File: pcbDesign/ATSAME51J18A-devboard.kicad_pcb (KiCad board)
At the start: 2 copper layers, 83.6 x 28.4 mm, 75 parts, among them IC1 MP9361DJ-LF-P, J1 Micro_SD_Card, J10 CAN, J11 Conn_01x32_Male, J2 USB C, J3 QWIIC, J4 S2B-PH-K-S(LF)(SN), J7 Conn_01x32_Male, SW1 RST, U1 TCAN1051GVDRQ1, U2 ATSAME51J18A-A, U3 MIC5219-5.0YMM, U4 LM27762, U5 TPS60501DGS, U7 BQ24074RGT, U8 BQ27441DRZR-G1B, Y1 32.768

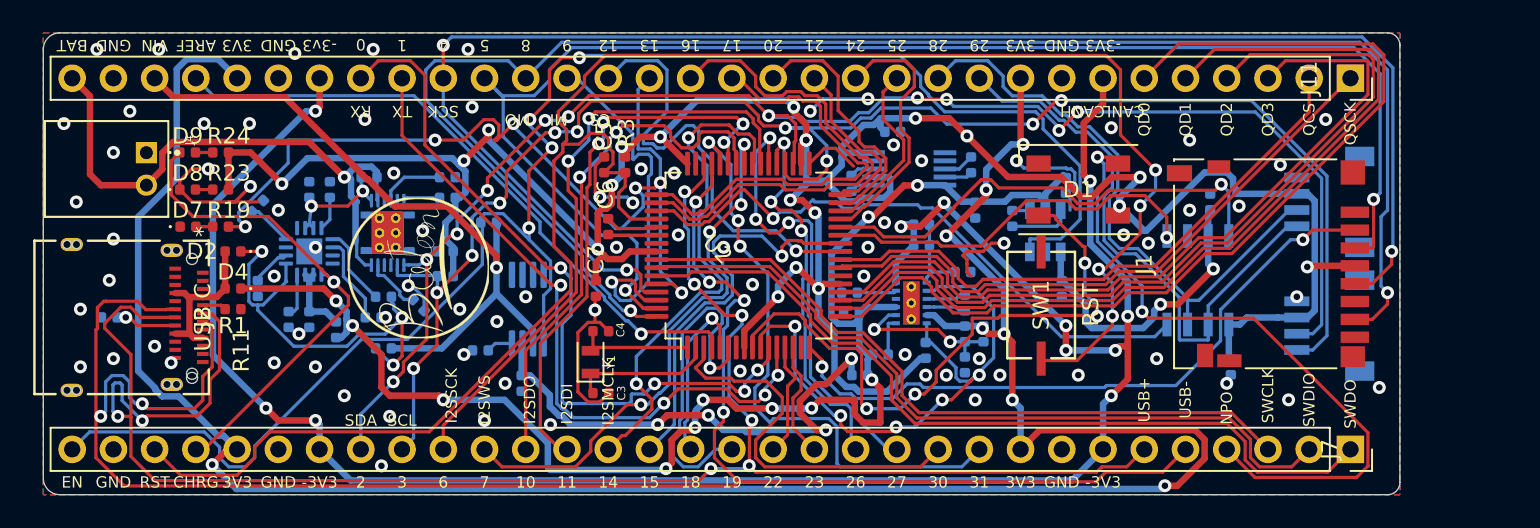
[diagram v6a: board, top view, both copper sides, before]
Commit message: Fixed some DRC errors
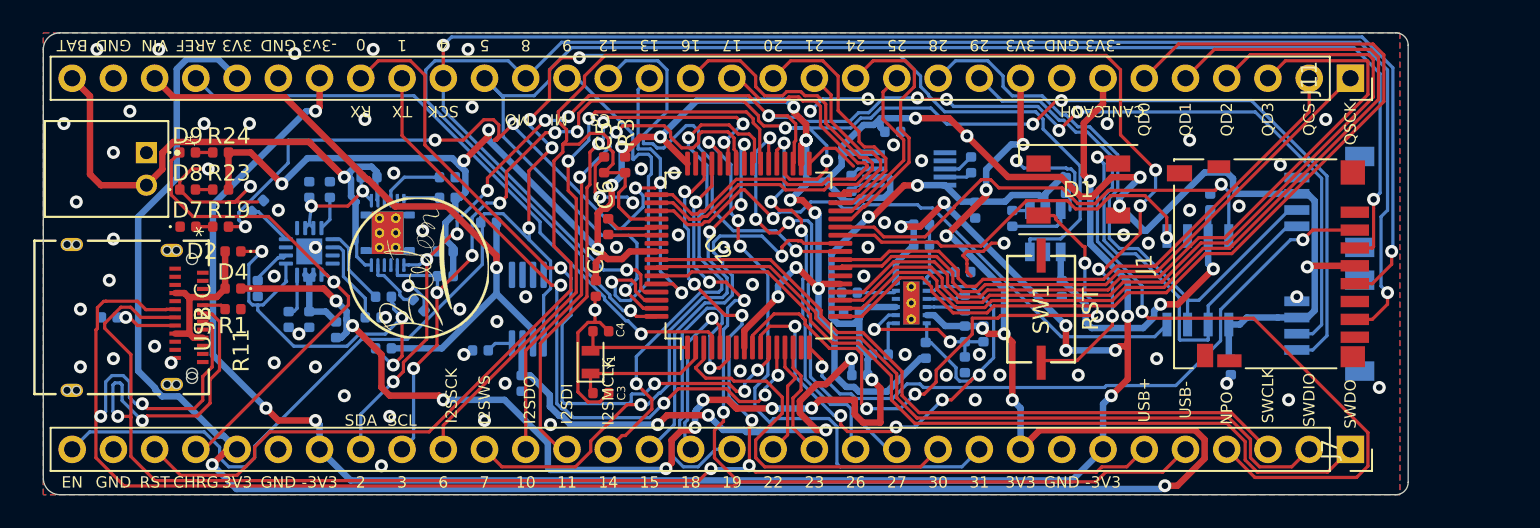
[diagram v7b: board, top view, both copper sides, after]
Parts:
- moved SW1 0.25 mm to (202.4, 128.5)
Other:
- board size 83.6 x 28.4 mm -> 84.1 x 28.4 mm
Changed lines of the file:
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@@
-(kicad_pcb (version 20171130) (host pcbnew "(5.1.6)-1")
+(kicad_pcb (version 20171130) (host pcbnew 5.1.5+dfsg1-2build2)
   (general
     (thickness 1.6)
     (drawings 93)
-    (tracks 2020)
+    (tracks 2019)
     (zones 0)
     (modules 75)
@@
   )
   (module "PTS636:PTS636 SM25F SMTR LFS" (layer F.Cu)
-    (at 202.438 128.27 90)
+    (at 202.438 128.524 90)
     (fp_text reference SW1 (at 0 0 90) (layer F.SilkS)
       (effects (font (size 1 1) (thickness 0.15)))
@@
   (gr_arc (start 141.986 112.522) (end 141.986 111.506) (angle -90) (layer Edge.Cuts) (width 0.05))
   (gr_arc (start 141.986 138.938) (end 140.97 138.938) (angle -90) (layer Edge.Cuts) (width 0.05))
-  (gr_line (start 141.986 111.506) (end 223.774 111.506) (layer Edge.Cuts) (width 0.05))
-  (gr_arc (start 223.774 139.192) (end 223.774 139.954) (angle -90) (layer Edge.Cuts) (width 0.05))
-  (gr_arc (start 223.774 112.268) (end 224.536 112.268) (angle -90) (layer Edge.Cuts) (width 0.05))
+  (gr_line (start 141.986 111.506) (end 224.282 111.506) (layer Edge.Cuts) (width 0.05))
+  (gr_arc (start 224.282 139.192) (end 224.282 139.954) (angle -90) (layer Edge.Cuts) (width 0.05))
+  (gr_arc (start 224.282 112.268) (end 225.044 112.268) (angle -90) (layer Edge.Cuts) (width 0.05))
   (gr_line (start 140.97 138.938) (end 140.97 112.522) (layer Edge.Cuts) (width 0.05))
-  (gr_line (start 223.774 139.954) (end 141.986 139.954) (layer Edge.Cuts) (width 0.05))
-  (gr_line (start 224.536 112.268) (end 224.536 139.192) (layer Edge.Cuts) (width 0.05))
+  (gr_line (start 224.282 139.954) (end 141.986 139.954) (layer Edge.Cuts) (width 0.05))
+  (gr_line (start 225.044 112.268) (end 225.044 139.192) (layer Edge.Cuts) (width 0.05))
   (via (at 193.344907 118.406298) (size 0.8) (drill 0.4) (layers F.Cu B.Cu) (net 1))
   (via (at 218.186 127.762) (size 0.8) (drill 0.4) (layers F.Cu B.Cu) (net 1))
@@
   (via (at 211.582 122.428) (size 0.8) (drill 0.4) (layers F.Cu B.Cu) (net 1))
   (via (at 214.63 122.174) (size 0.8) (drill 0.4) (layers F.Cu B.Cu) (net 1))
-  (via (at 206.756 117.348) (size 0.8) (drill 0.4) (layers F.Cu B.Cu) (net 1))
+  (via (at 206.502 117.094) (size 0.8) (drill 0.4) (layers F.Cu B.Cu) (net 1))
   (via (at 191.516 126.492) (size 0.8) (drill 0.4) (layers F.Cu B.Cu) (net 1))
   (via (at 194.056 131.318) (size 0.8) (drill 0.4) (layers F.Cu B.Cu) (net 1))
@@
   (via (at 196.596 132.588) (size 0.8) (drill 0.4) (layers F.Cu B.Cu) (net 1))
   (via (at 195.326 132.588) (size 0.8) (drill 0.4) (layers F.Cu B.Cu) (net 1))
-  (via (at 198.628 131.572) (size 0.8) (drill 0.4) (layers F.Cu B.Cu) (net 1))
+  (via (at 198.628 131.318) (size 0.8) (drill 0.4) (layers F.Cu B.Cu) (net 1))
   (via (at 183.896 132.334) (size 0.8) (drill 0.4) (layers F.Cu B.Cu) (net 1))
   (via (at 191.77 124.714) (size 0.8) (drill 0.4) (layers F.Cu B.Cu) (net 1))
@@
   (segment (start 180.647367 123.318255) (end 181.533091 123.318255) (width 0.2) (layer F.Cu) (net 75))
   (segment (start 178.7415 122.472) (end 179.801112 122.472) (width 0.2) (layer F.Cu) (net 75))
-  (segment (start 187.622504 122.536001) (end 186.327999 122.536001) (width 0.2) (layer B.Cu) (net 75))
-  (segment (start 188.354493 121.804012) (end 187.622504 122.536001) (width 0.2) (layer B.Cu) (net 75))
+  (segment (start 190.208076 122.31102) (end 189.817056 121.92) (width 0.2) (layer B.Cu) (net 75))
   (segment (start 186.327999 122.536001) (end 185.928 122.936) (width 0.2) (layer B.Cu) (net 75))
-  (segment (start 188.425872 121.804012) (end 188.354493 121.804012) (width 0.2) (layer B.Cu) (net 75))
-  (segment (start 209.434139 130.221011) (end 203.674955 130.221011) (width 0.2) (layer B.Cu) (net 75))
-  (segment (start 210.185 129.47015) (end 209.434139 130.221011) (width 0.2) (layer B.Cu) (net 75))
-  (segment (start 195.025038 122.293002) (end 194.825047 122.093011) (width 0.2) (layer B.Cu) (net 75))
-  (segment (start 191.517933 122.093011) (end 191.299923 122.311021) (width 0.2) (layer B.Cu) (net 75))
-  (segment (start 203.674955 130.221011) (end 195.746946 122.293002) (width 0.2) (layer B.Cu) (net 75))
-  (segment (start 195.746946 122.293002) (end 195.025038 122.293002) (width 0.2) (layer B.Cu) (net 75))
-  (segment (start 189.817056 121.92) (end 188.468 121.92) (width 0.2) (layer B.Cu) (net 75))
   (segment (start 191.299923 122.311021) (end 190.208076 122.31102) (width 0.2) (layer B.Cu) (net 75))
-  (segment (start 190.208076 122.31102) (end 189.817056 121.92) (width 0.2) (layer B.Cu) (net 75))
+  (segment (start 188.238505 121.92) (end 187.622504 122.536001) (width 0.2) (layer B.Cu) (net 75))
   (segment (start 194.825047 122.093011) (end 191.517933 122.093011) (width 0.2) (layer B.Cu) (net 75))
+  (segment (start 187.622504 122.536001) (end 186.327999 122.536001) (width 0.2) (layer B.Cu) (net 75))
+  (segment (start 191.517933 122.093011) (end 191.299923 122.311021) (width 0.2) (layer B.Cu) (net 75))
+  (segment (start 195.025038 122.293002) (end 194.825047 122.093011) (width 0.2) (layer B.Cu) (net 75))
+  (segment (start 195.746946 122.293002) (end 195.025038 122.293002) (width 0.2) (layer B.Cu) (net 75))
+  (segment (start 203.674955 130.221011) (end 195.746946 122.293002) (width 0.2) (layer B.Cu) (net 75))
+  (segment (start 209.434139 130.221011) (end 203.674955 130.221011) (width 0.2) (layer B.Cu) (net 75))
+  (segment (start 189.817056 121.92) (end 188.238505 121.92) (width 0.2) (layer B.Cu) (net 75))
+  (segment (start 210.185 129.47015) (end 209.434139 130.221011) (width 0.2) (layer B.Cu) (net 75))
   (segment (start 213.995 121.297148) (end 213.531466 120.833614) (width 0.2) (layer B.Cu) (net 76))
   (via (at 213.531466 120.833614) (size 0.8) (drill 0.4) (layers F.Cu B.Cu) (net 76))

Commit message: Finnished routing board prototype(v0.2)
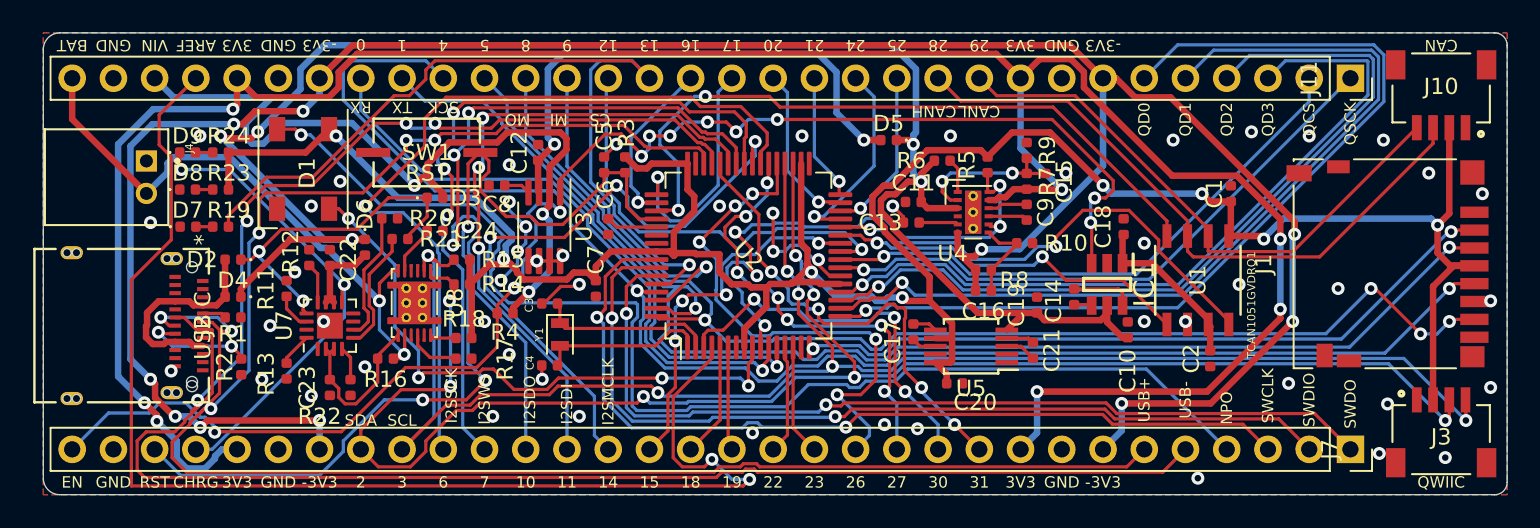
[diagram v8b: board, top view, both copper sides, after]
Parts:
- C1, C10, C11, C12, C13, C14, C15, C16, C17, C18, C19, C2, C20, C21, C22, C23, C24, C8, C9, D3, D5, D6, IC1, J10, J3, R10, R11, R12, R13, R14, R15, R16, R17, R18, R2, R20, R21, R22, R4, R5, R6, R7, R8, R9, U1, U3, U4, U5, U7, U8: moved to F.Cu
- G***: moved to B.Cu
- moved D1 47.8 mm to (157.0, 119.9), turned to 270 degrees
- moved SW1 39.1 mm to (164.6, 118.9), turned to 180 degrees
- moved G*** 20.6 mm to (184.7, 125.2), turned to 270 degrees
- moved C20 16.0 mm to (197.1, 133.1)
- moved D5 14.6 mm to (193.0, 118.1)
- moved C12 14.3 mm to (171.4, 118.9), turned to 90 degrees
- moved R9 13.7 mm to (201.5, 118.7), turned to 90 degrees
- moved R6 12.5 mm to (196.3, 119.4)
- moved R22 12.3 mm to (159.9, 133.3), turned to 90 degrees
- moved C23 12.3 mm to (158.6, 133.3), turned to 270 degrees
- moved C21 12.0 mm to (201.9, 131.1), turned to 270 degrees
- moved R5 12.0 mm to (199.1, 119.6), turned to 90 degrees
- moved U5 11.6 mm to (198.1, 130.8)
- moved R16 11.2 mm to (162.1, 131.6)
- moved R17 11.2 mm to (166.9, 131.6)
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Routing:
- net RST: track 116.0 -> 57.5 mm, vias 4 -> 3
- net AREF: track 39.7 -> 79.1 mm, vias 1 -> 2
- net NEOPIXEL_DOUT: track 41.2 -> 76.0 mm, vias 2 -> 1
- net GND: track 48.5 -> 21.7 mm, vias 81 -> 54
- net 8[MI]: track 100.8 -> 75.1 mm, vias 2 -> 4
- net VBUS_-3V3_CH2_REG: track 129.7 -> 150.9 mm, vias 11 -> 10
- net 16: track 31.2 -> 10.5 mm, vias 0 -> 1
- net VBUS_NREG: track 88.2 -> 105.8 mm, vias 11 -> 5
- net 19: track 21.1 -> 6.37 mm, vias 1 -> 0
- net 10[I2SDO]: track 32.6 -> 46.2 mm, vias 2 -> 3
- net EN: track 102.8 -> 89.8 mm, vias 4 -> 11
- net 6[I2SSCK]: track 37.9 -> 49.7 mm, vias 2 -> 1
- net 17: track 26.5 -> 14.9 mm, vias 0 -> 1
- net SWCLK: track 43.6 -> 54.7 mm, vias 0 -> 2
- net 7[I2SWS]: track 34.0 -> 44.1 mm, vias 4 -> 3
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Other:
- board size 84.1 x 28.4 mm -> 90.2 x 28.4 mm
- board text added: "BAT+"
- board text added: "BAT-"
- board text added: "CAN"
- board text added: "QWIIC"
